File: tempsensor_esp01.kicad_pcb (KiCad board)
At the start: 2 copper layers, 33 x 34 mm, 29 parts, among them J1 Stemma QT, J2 USB_C_Receptacle_USB2.0, SW1 SW_Push, SW2 SW_Push, U1 ESP-01v090, U2 SHT40-AD1B-R2, U3 DPS310, U4 MIC5205-3.3YM5, U5 FT234XD-R

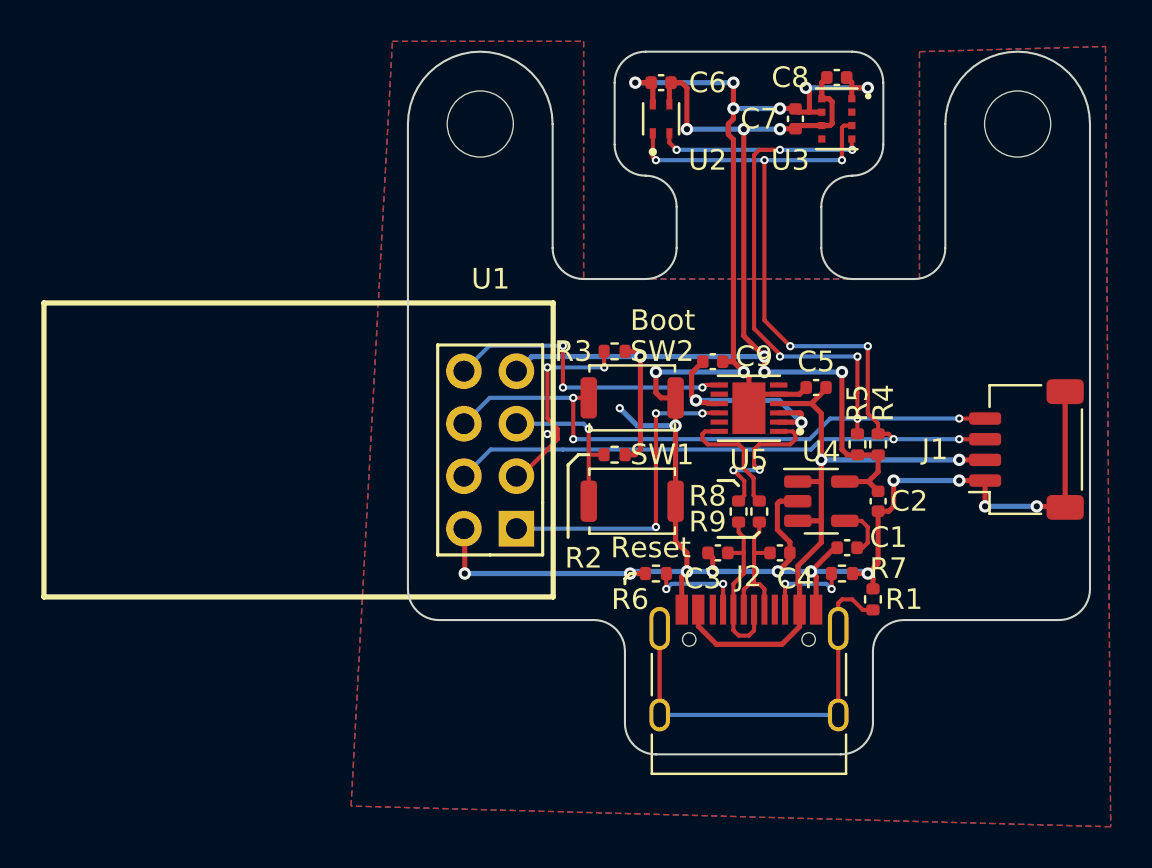
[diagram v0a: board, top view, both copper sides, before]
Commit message: redesign using CH340E
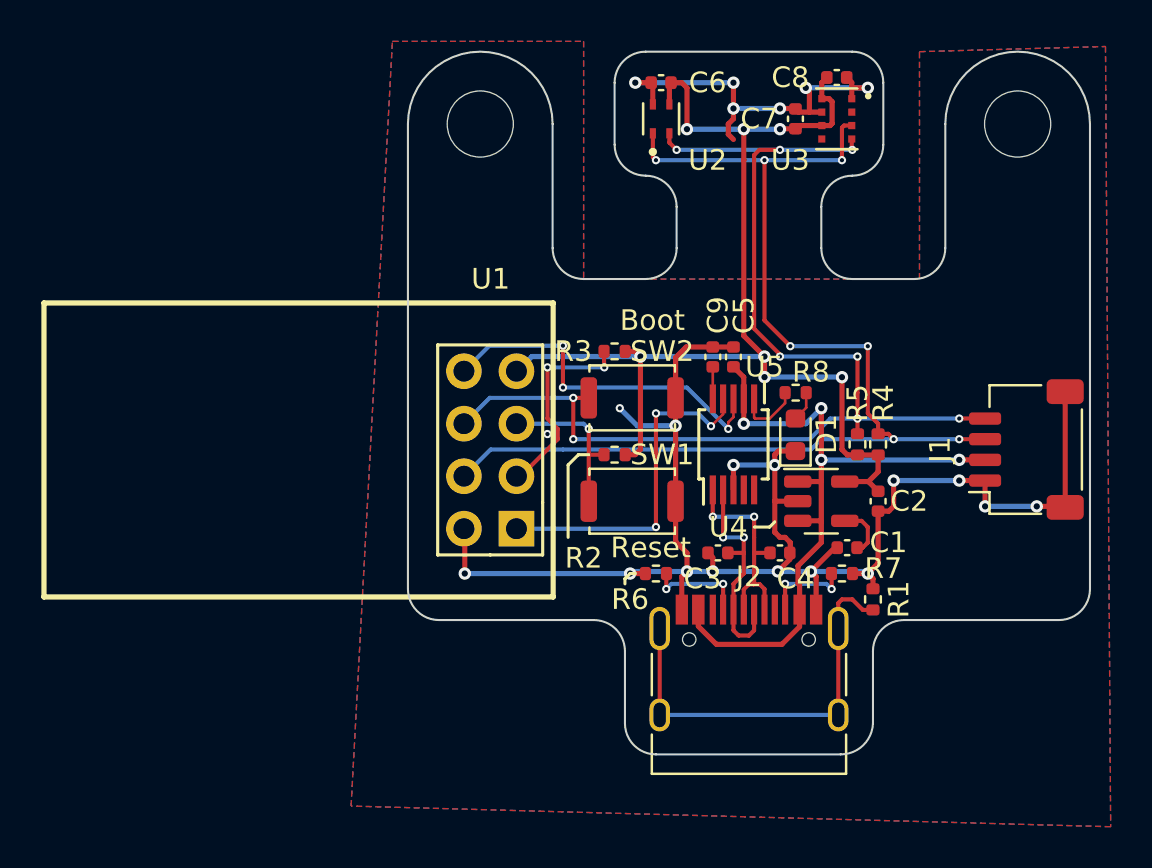
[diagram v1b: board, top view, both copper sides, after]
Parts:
- removed R9: 27R, Resistor_SMD:R_0402_1005Metric
- added D1: Red, LED_SMD:LED_0603_1608Metric, F.Cu at (143.2, 85.3)
- H1, H2: value MountingHole -> M3
- R8: value 27R -> 220R
- U5: value FT234XD-R -> CH340E; footprint ! FT234XD-R:SON45P300X300X80-13N -> Package_SO:MSOP-10_3x3mm_P0.5mm
- moved R8 6.38 mm to (143.3, 83.2), turned to 0 degrees
- moved C5 5.21 mm to (139.2, 81.5), turned to -90 degrees
- moved U5 1.90 mm to (140.2, 85.8), turned to 90 degrees
- moved C9 1.03 mm to (140.2, 81.5), turned to 90 degrees
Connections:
- C5 pad 1: +5V -> GND
- C5 pad 2: GND -> Net-(C5-Pad2)
- C9 pad 1: /FT_3V3 -> +5V
- R8 pad 1: D- -> Net-(U5-Pad6)
- R8 pad 2: /FT_USBD- -> Net-(D1-Pad2)
- U5 pad 1: /FT_USBD- -> D+
- U5 pad 10: /UTXD -> Net-(C5-Pad2)
- U5 pad 2: /FT_3V3 -> D-
- U5 pad 3: /FT_3V3 -> GND
- U5 pad 4: +5V -> unconnected-(U5-Pad4)
- U5 pad 5: GND -> unconnected-(U5-Pad5)
- U5 pad 6: unconnected-(U5-Pad6) -> Net-(U5-Pad6)
- U5 pad 7: /URXD -> +5V
- U5 pad 8: unconnected-(U5-Pad8) -> /URXD
- U5 pad 9: /FT_3V3 -> /UTXD
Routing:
- net /FT_3V3: track 11.6 -> 0.00 mm, vias 2 -> 0
- net GND: track 112.2 -> 100.8 mm
- net /FT_USBD-: track 7.54 -> 0.00 mm, vias 2 -> 0
- net /FT_USBD+: track 6.12 -> 0.00 mm
- net +5V: track 30.8 -> 34.7 mm, vias 2 -> 4
- net D+: track 7.06 -> 10.5 mm, vias 0 -> 2
- net Net-(U5-Pad6): track 0.00 -> 3.23 mm
- net /URXD: track 14.9 -> 17.7 mm
- net D-: track 8.53 -> 11.0 mm, vias 0 -> 2
- net Net-(C5-Pad2): track 0.00 -> 1.55 mm
- net Net-(D1-Pad2): track 0.00 -> 1.47 mm
- net /UTXD: track 15.4 -> 16.8 mm

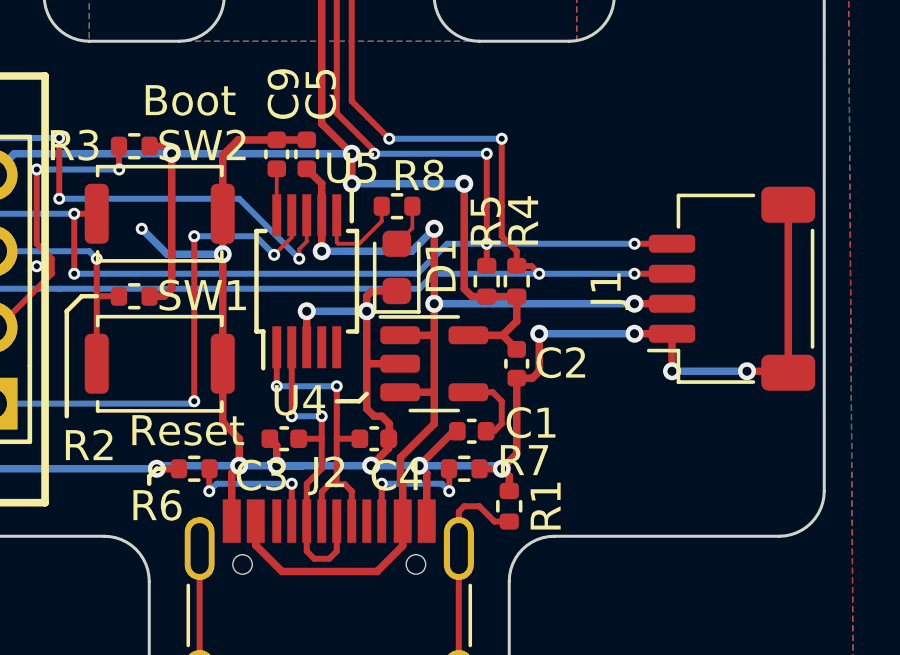
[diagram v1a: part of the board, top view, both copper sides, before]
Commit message: change power regulator
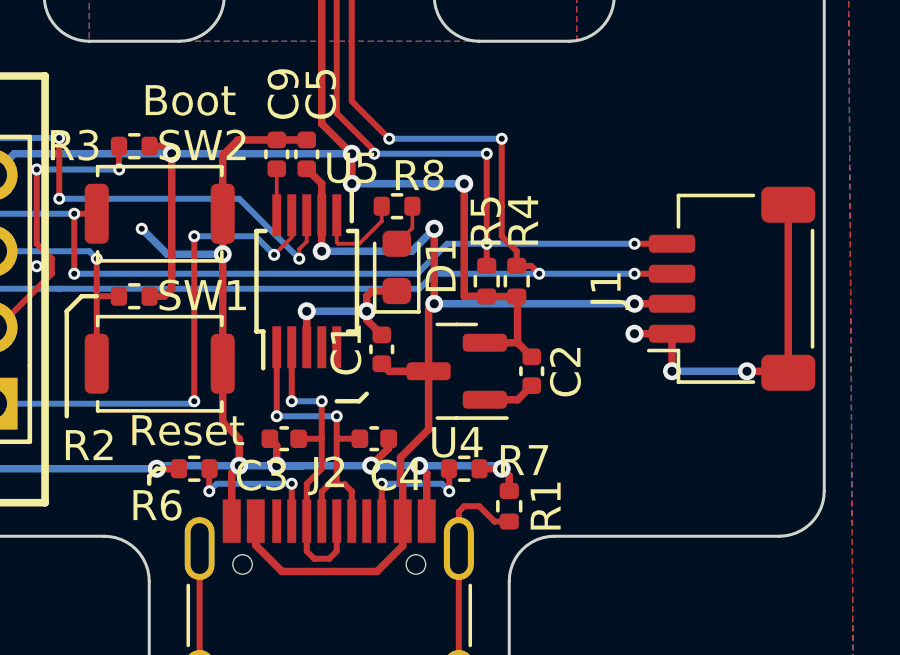
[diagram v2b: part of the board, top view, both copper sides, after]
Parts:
- C1: value 470p -> 1u
- C2: value 2.2u -> 1u
- U4: value MIC5205-3.3YM5 -> XC6206P332MR; footprint Package_TO_SOT_SMD:SOT-23-5 -> Package_TO_SOT_SMD:SOT-23
- moved C1 4.06 mm to (142.8, 88.0), turned to 90 degrees
- moved U4 0.79 mm to (145.2, 88.8), turned to 180 degrees
- moved C2 0.56 mm to (147.8, 88.8)
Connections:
- C1 pad 1: /REG_BP -> +5V
- U4 pad 1: +5V -> GND
- U4 pad 2: GND -> +3V3
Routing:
- net GND: track 100.8 -> 87.5 mm, vias 22 -> 21
- net /REG_BP: track 2.61 -> 0.00 mm
- net +5V: track 34.7 -> 34.1 mm
